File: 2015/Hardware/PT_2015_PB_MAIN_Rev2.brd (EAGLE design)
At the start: 137.2 x 166.4 mm, 135 parts, among them Q1 Q_ACS711LC, Q11 Q_IRFS7437PbF, Q12 2N7002, Q14 Q_IRFS7437PbF, Q16 Q_IRFS7437PbF, Q18 Q_FDT86102LZ, Q20 Q_IRFS7437PbF, Q4 Q_ACS711LC, Q5 Q_ACS711LC, Q6 Q_IRFS7437PbF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

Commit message: can't remember
made some small changes
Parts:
- moved C3 37.5 mm to (61.6, 80.0)
- moved C2 19.7 mm to (61.6, 60.3)
- moved C1 17.8 mm to (61.6, 42.5)
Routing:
- net PRIMARY-VMEAS: track 7.16 -> 8.20 mm
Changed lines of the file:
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@@
 <element name="VADER-5V-EXT" library="MRDT-2015-PowerBoard" package="R_PDSS-T7" value="Q_PTN78020WAH" x="103.505" y="88.9"/>
 <element name="DOOKU-12V-CRIT" library="MRDT-2015-PowerBoard" package="R_PDSS-T7" value="Q_PTN78020WAH" x="103.505" y="63.5"/>
-<element name="C1" library="MRDT-2014-All" package="C_12.5MM" value="1mF" x="61.595" y="60.325"/>
-<element name="C2" library="MRDT-2014-All" package="C_12.5MM" value="1mF" x="61.595" y="80.01"/>
-<element name="C3" library="MRDT-2014-All" package="C_12.5MM" value="1mF" x="61.595" y="42.545"/>
+<element name="C2" library="MRDT-2014-All" package="C_12.5MM" value="1mF" x="61.595" y="60.325"/>
+<element name="C3" library="MRDT-2014-All" package="C_12.5MM" value="1mF" x="61.595" y="80.01"/>
+<element name="C1" library="MRDT-2014-All" package="C_12.5MM" value="1mF" x="61.595" y="42.545"/>
 <element name="C4" library="MRDT-2014-All" package="C_12.5MM" value="1mF" x="60.96" y="103.505"/>
 <element name="C5" library="resistor" package="C1206" value=".1µF" x="45.72" y="1.778" rot="R180"/>
@@
 <contactref element="C15" pad="1"/>
 <contactref element="C4" pad="-"/>
+<contactref element="C1" pad="-"/>
 <contactref element="C3" pad="-"/>
 <contactref element="C2" pad="-"/>
-<contactref element="C1" pad="-"/>
 <contactref element="U$2" pad="2"/>
 <contactref element="C11" pad="2"/>
@@
 <contactref element="L5" pad="3"/>
 <contactref element="C10" pad="2"/>
-<contactref element="C1" pad="+"/>
 <contactref element="C2" pad="+"/>
 <contactref element="C3" pad="+"/>
+<contactref element="C1" pad="+"/>
 <contactref element="C4" pad="+"/>
 <contactref element="U$14" pad="1"/>
@@
 <wire x1="128.905" y1="11.43" x2="128.905" y2="27.94" width="1.016" layer="16"/>
 <via x="121.793" y="31.623" extent="1-16" drill="0.3302"/>
-<wire x1="121.793" y1="31.623" x2="105.41" y2="31.496" width="0.8128" layer="1"/>
-<wire x1="105.41" y1="31.496" x2="103.759" y2="33.147" width="0.8128" layer="1"/>
-<wire x1="103.759" y1="33.147" x2="103.759" y2="37.846" width="0.8128" layer="1"/>
+<wire x1="121.793" y1="31.623" x2="105.41" y2="31.623" width="0.8128" layer="1"/>
+<wire x1="105.41" y1="31.623" x2="103.759" y2="33.274" width="0.8128" layer="1"/>
+<wire x1="103.759" y1="33.274" x2="103.759" y2="37.846" width="0.8128" layer="1"/>
 <wire x1="103.759" y1="37.846" x2="102.362" y2="39.243" width="0.8128" layer="16"/>
 <wire x1="102.362" y1="39.243" x2="88.265" y2="39.243" width="0.8128" layer="16"/>
@@
 <contactref element="U$1" pad="19"/>
 <wire x1="82.067" y1="32.258" x2="84.938" y2="32.258" width="0.4064" layer="1"/>
-<wire x1="87.63" y1="29.083" x2="85.09" y2="31.623" width="0.4064" layer="1"/>
-<wire x1="85.09" y1="31.623" x2="85.09" y2="32.106" width="0.4064" layer="1"/>
 <wire x1="85.09" y1="32.106" x2="84.938" y2="32.258" width="0.4064" layer="1"/>
+<wire x1="85.09" y1="32.106" x2="85.09" y2="30.861" width="0.4064" layer="1"/>
+<wire x1="85.09" y1="30.861" x2="85.471" y2="30.48" width="0.4064" layer="1"/>
+<wire x1="85.471" y1="30.48" x2="87.249" y2="30.48" width="0.4064" layer="1"/>
+<wire x1="87.249" y1="30.48" x2="87.63" y2="30.099" width="0.4064" layer="1"/>
+<wire x1="87.63" y1="30.099" x2="87.63" y2="29.083" width="0.4064" layer="1"/>
 </signal>
 <signal name="M2-IMEAS">
@@
 <contactref element="Q5" pad="7"/>
 <contactref element="U$1" pad="1"/>
-<wire x1="120.65" y1="46.863" x2="123.825" y2="48.26" width="0.4064" layer="1"/>
-<wire x1="123.825" y1="48.26" x2="128.778" y2="48.26" width="0.4064" layer="1"/>
+<wire x1="120.65" y1="46.863" x2="122.047" y2="48.26" width="0.4064" layer="1"/>
+<wire x1="122.047" y1="48.26" x2="128.778" y2="48.26" width="0.4064" layer="1"/>
 <wire x1="128.778" y1="48.26" x2="130.175" y2="49.657" width="0.4064" layer="1"/>
 <wire x1="130.175" y1="49.657" x2="130.175" y2="53.915" width="0.4064" layer="1"/>

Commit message: Oh yeah BTW this is basically done
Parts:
- moved BATT-POS 0.25 mm to (62.4, 13.5)
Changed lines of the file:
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@@
 <element name="C10" library="resistor" package="C1206" value="" x="81.153" y="52.197" rot="R180"/>
 <element name="C14" library="resistor" package="C1206" value="2.2µF" x="81.28" y="68.58" rot="R270"/>
-<element name="BATT-POS" library="MRDT-2015-PowerBoard" package="LARGE_TERMINAL_HOLE" value="TERMINAL_HOLE" x="62.103" y="13.462"/>
+<element name="BATT-POS" library="MRDT-2015-PowerBoard" package="LARGE_TERMINAL_HOLE" value="TERMINAL_HOLE" x="62.357" y="13.462"/>
 <element name="BATT-NEG" library="MRDT-2015-PowerBoard" package="LARGE_TERMINAL_HOLE" value="TERMINAL_HOLE" x="93.98" y="13.462"/>
 <element name="Q6" library="MRDT-2015-PowerBoard" package="D2PACK" value="Q_IRFS7437PbF" x="29.21" y="7.62" rot="R270"/>

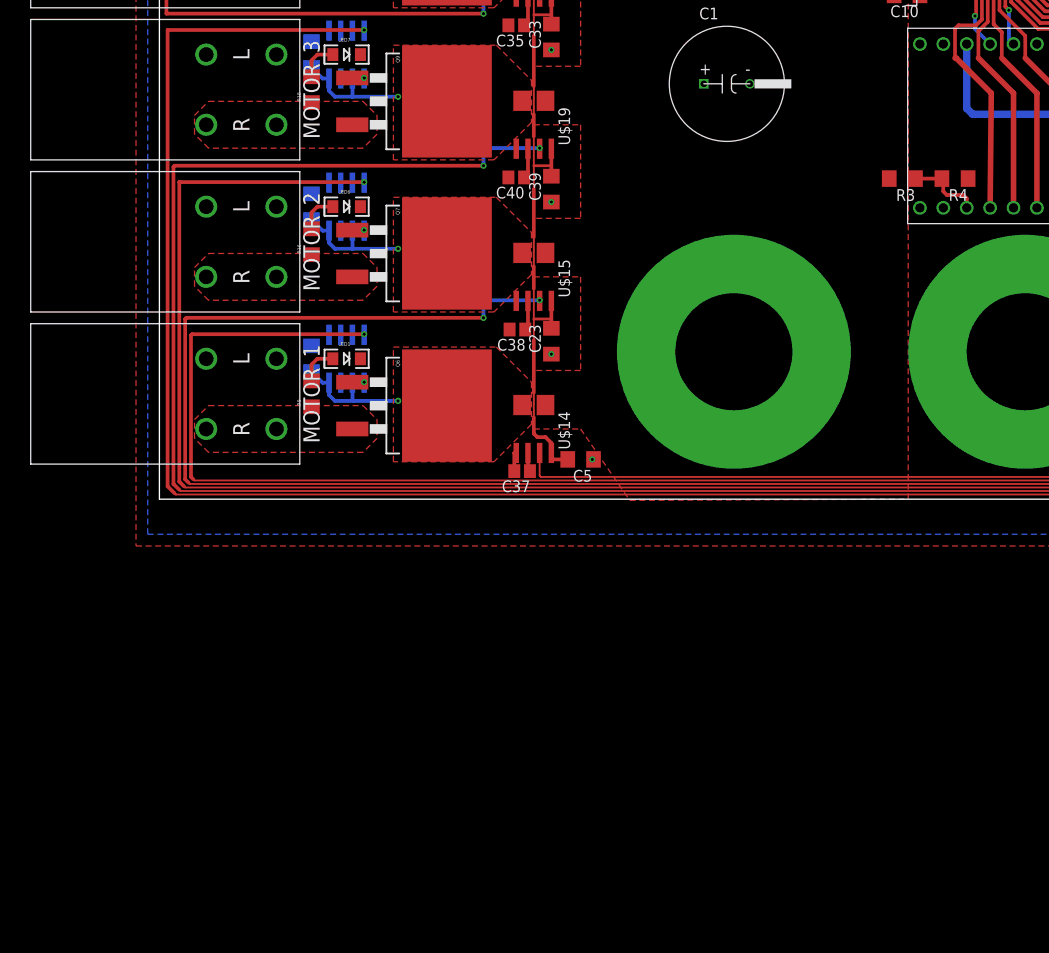
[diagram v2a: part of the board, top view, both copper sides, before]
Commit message: Added a buzzer and LEDs to schematic
Parts are not placed yet.
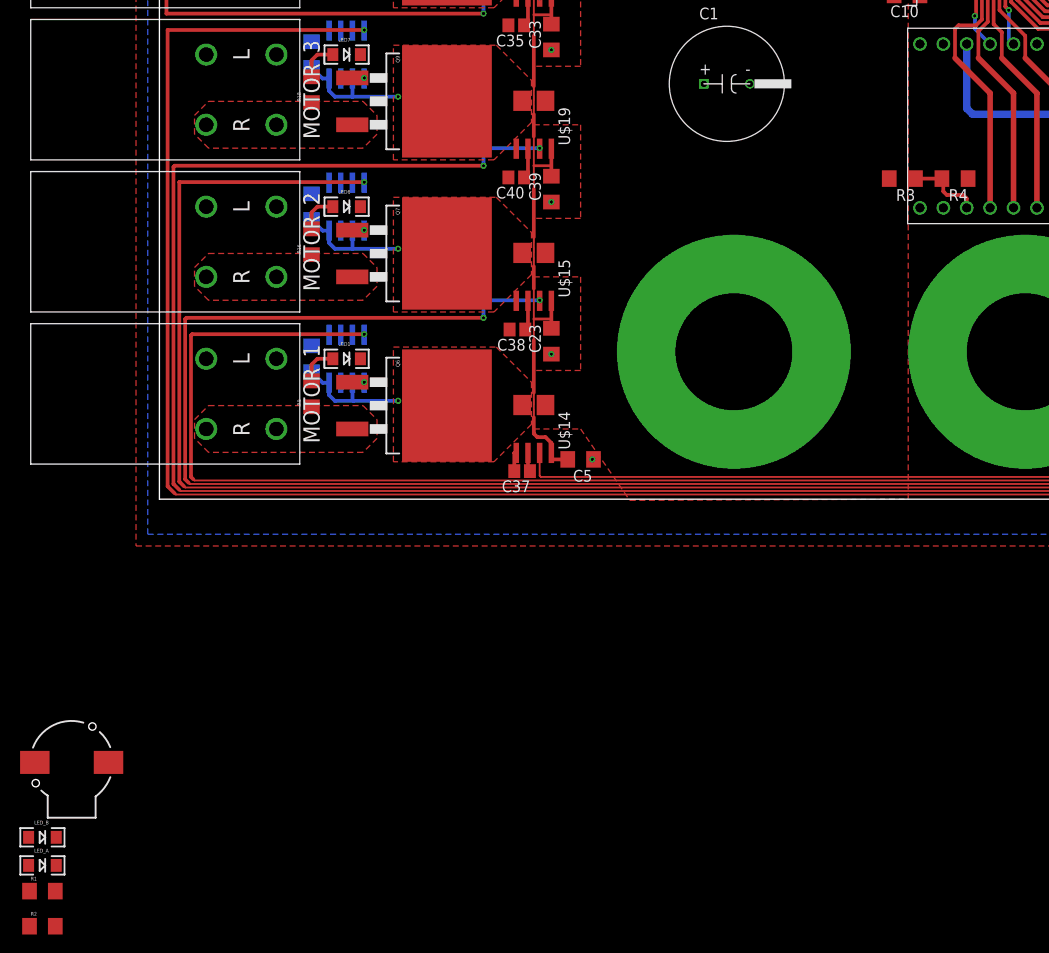
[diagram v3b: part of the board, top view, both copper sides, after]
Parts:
- added LED_A, LED_B: (no value), SparkFun-LED:LED-1206
- added R1, R2: 1kΩ, SparkFun-Passives:1206
- added SG1: BUZZERSMD2, SparkFun-Electromechanical:BUZZER-CCV
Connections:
- new net BUZZER: SG1.+, U$1.11
- new net LED_A: R1.1, U$1.9
- new net LED_B: R2.1, U$1.10
- new net N$32: LED_A.A, R1.2
- new net N$33: LED_B.A, R2.2
- net GND: now also LED_A.C, LED_B.C, SG1.-
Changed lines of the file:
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@@
 <attribute name="DIGIKEY_PN" value="732-2769-ND" x="-128.143" y="-38.735" size="1.778" layer="27" rot="R270" display="off"/>
 </element>
+<element name="SG1" library="SparkFun-Electromechanical" package="BUZZER-CCV" value="BUZZERSMD2" x="-9.525" y="-31.115"/>
+<element name="LED_B" library="SparkFun-LED" package="LED-1206" value="" x="-12.7" y="-39.243"/>
+<element name="LED_A" library="SparkFun-LED" package="LED-1206" value="" x="-12.7" y="-42.291"/>
+<element name="R1" library="SparkFun-Passives" package="1206" value="1kΩ" x="-12.7" y="-45.085"/>
+<element name="R2" library="SparkFun-Passives" package="1206" value="1kΩ" x="-12.7" y="-48.895"/>
 </elements>
 <signals>
@@
 <wire x1="38.735" y1="2.48" x2="38.52" y2="2.48" width="0.4064" layer="1"/>
 <wire x1="38.52" y1="2.48" x2="38.52" y2="0.508" width="0.4064" layer="1"/>
+<contactref element="SG1" pad="-"/>
+<contactref element="LED_A" pad="C"/>
+<contactref element="LED_B" pad="C"/>
+<wire x1="-11.2" y1="-39.243" x2="-11.2" y2="-42.291" width="0" layer="19" extent="1-1"/>
+<wire x1="-13.525" y1="-31.115" x2="-11.2" y2="-39.243" width="0" layer="19" extent="1-1"/>
+<wire x1="5.08" y1="12.7" x2="-13.525" y2="-31.115" width="0" layer="19" extent="1-1"/>
 </signal>
 <signal name="V_BATT">
@@
 <wire x1="86.741" y1="48.895" x2="86.36" y2="48.514" width="0.4064" layer="1"/>
 <wire x1="86.36" y1="48.514" x2="86.36" y2="45.339" width="0.4064" layer="1"/>
-<wire x1="90.17" y1="29.083" x2="90.297" y2="41.529" width="0.6096" layer="1"/>
-<wire x1="90.297" y1="41.529" x2="86.487" y2="45.339" width="0.6096" layer="1"/>
-<wire x1="86.487" y1="45.339" x2="86.36" y2="45.339" width="0.6096" layer="1"/>
+<wire x1="90.17" y1="29.083" x2="90.17" y2="41.529" width="0.6096" layer="1"/>
+<wire x1="90.17" y1="41.529" x2="86.36" y2="45.339" width="0.6096" layer="1"/>
 <wire x1="103.378" y1="100.33" x2="102.616" y2="99.568" width="0.4064" layer="1"/>
 <wire x1="67.945" y1="141.351" x2="67.183" y2="140.589" width="0.4064" layer="1"/>
@@
 <signal name="N$13">
 </signal>
+<signal name="BUZZER">
+<contactref element="SG1" pad="+"/>
+<contactref element="U$1" pad="11"/>
+<wire x1="-5.525" y1="-31.115" x2="95.25" y2="46.863" width="0" layer="19" extent="1-1"/>
+</signal>
+<signal name="N$32">
+<contactref element="LED_A" pad="A"/>
+<contactref element="R1" pad="2"/>
+<wire x1="-11.3" y1="-45.085" x2="-14.2" y2="-42.291" width="0" layer="19" extent="1-1"/>
+</signal>
+<signal name="N$33">
+<contactref element="LED_B" pad="A"/>
+<contactref element="R2" pad="2"/>
+<wire x1="-14.2" y1="-39.243" x2="-11.3" y2="-48.895" width="0" layer="19" extent="1-1"/>
+</signal>
+<signal name="LED_B">
+<contactref element="U$1" pad="10"/>
+<contactref element="R2" pad="1"/>
+<wire x1="-14.1" y1="-48.895" x2="97.79" y2="46.863" width="0" layer="19" extent="1-1"/>
+</signal>
+<signal name="LED_A">
+<contactref element="U$1" pad="9"/>
+<contactref element="R1" pad="1"/>
+<wire x1="-14.1" y1="-45.085" x2="100.33" y2="46.863" width="0" layer="19" extent="1-1"/>
+</signal>
 </signals>

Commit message: Fixed the triangle thing
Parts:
- removed LED_A, LED_B: (no value), SparkFun-LED:LED-1206
- removed R1, R2: 1kΩ, SparkFun-Passives:1206
- removed SG1: BUZZERSMD2, SparkFun-Electromechanical:BUZZER-CCV
- moved C3 37.5 mm to (61.6, 42.5)
- moved C2 19.7 mm to (61.6, 80.0)
- moved C1 17.8 mm to (61.6, 60.3)
- moved BATT-POS 0.25 mm to (62.1, 13.5)
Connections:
- removed net BUZZER: SG1.+, U$1.11
- removed net LED_A: R1.1, U$1.9
- removed net LED_B: R2.1, U$1.10
- removed net N$32: LED_A.A, R1.2
- removed net N$33: LED_B.A, R2.2
- net GND: no longer LED_A.C, LED_B.C, SG1.-
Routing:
- net ARM_P-SIG: track 220.4 -> 211.9 mm
- net ARM_P-IMEAS: track 292.3 -> 285.0 mm
- net AUX_P-IMEAS: track 316.7 -> 310.2 mm
- net M6-IMEAS: track 335.3 -> 329.7 mm
- net M5-IMEAS: track 354.7 -> 350.1 mm
- net M4-IMEAS: track 386.4 -> 382.7 mm
- net AUX_P-SIG: track 282.8 -> 280.2 mm
- net GND: track 2.32 -> 0.13 mm
- net M6-SIG: track 306.1 -> 304.5 mm
- net PRIMARY-VMEAS: track 8.20 -> 7.16 mm
- net M5-SIG: track 326.8 -> 326.3 mm

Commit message: init commit
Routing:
- net ARM_P-SIG: track 211.9 -> 185.9 mm
- net ARM_P-IMEAS: track 285.0 -> 259.2 mm
- net AUX_P-IMEAS: track 310.2 -> 284.6 mm
- net M6-IMEAS: track 329.7 -> 304.4 mm
- net M5-IMEAS: track 350.1 -> 325.0 mm
- net M4-IMEAS: track 382.7 -> 357.8 mm
- net AUX_P-SIG: track 280.2 -> 255.4 mm
- net M6-SIG: track 304.5 -> 280.3 mm
- net M5-SIG: track 326.3 -> 302.5 mm
- net +5V: track 629.7 -> 606.3 mm
- net 12V-IMEAS: track 289.1 -> 284.3 mm
- net M4-SIG: track 352.8 -> 350.4 mm
- net GND: vias 26 -> 16
- removed copper zone on layer 1, net N$7

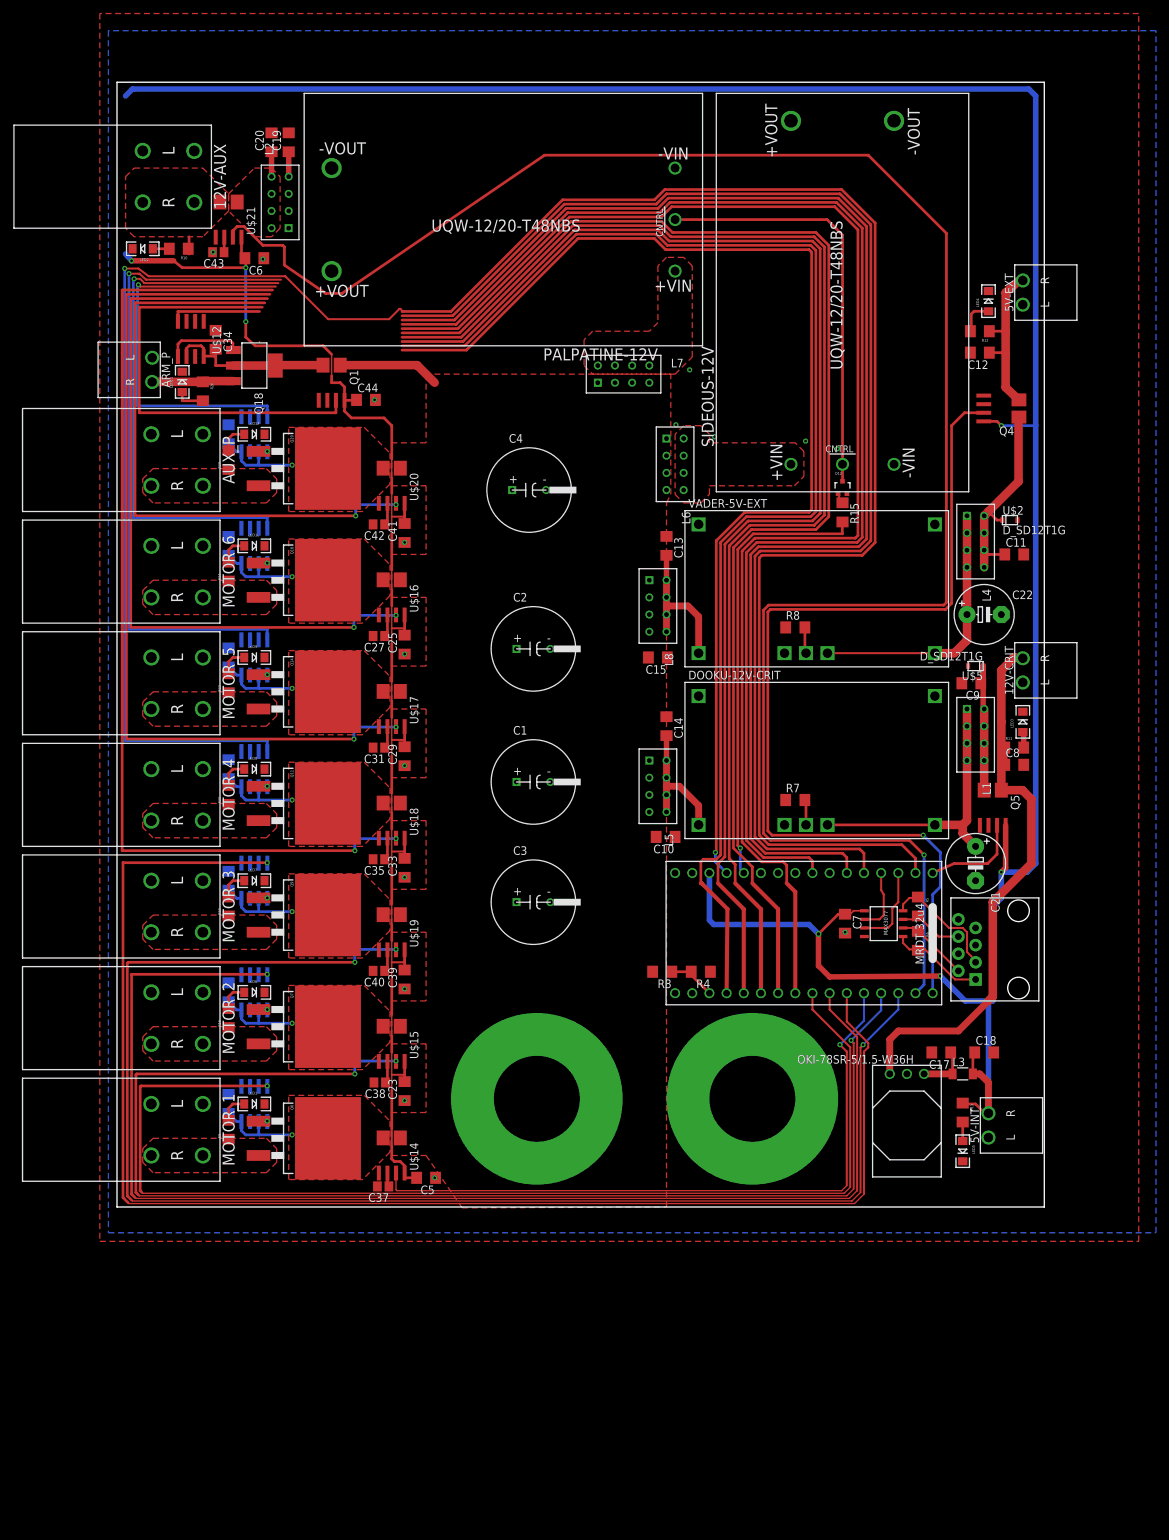
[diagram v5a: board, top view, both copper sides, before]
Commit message: rou
is my eagle command for route because fuck buttons.
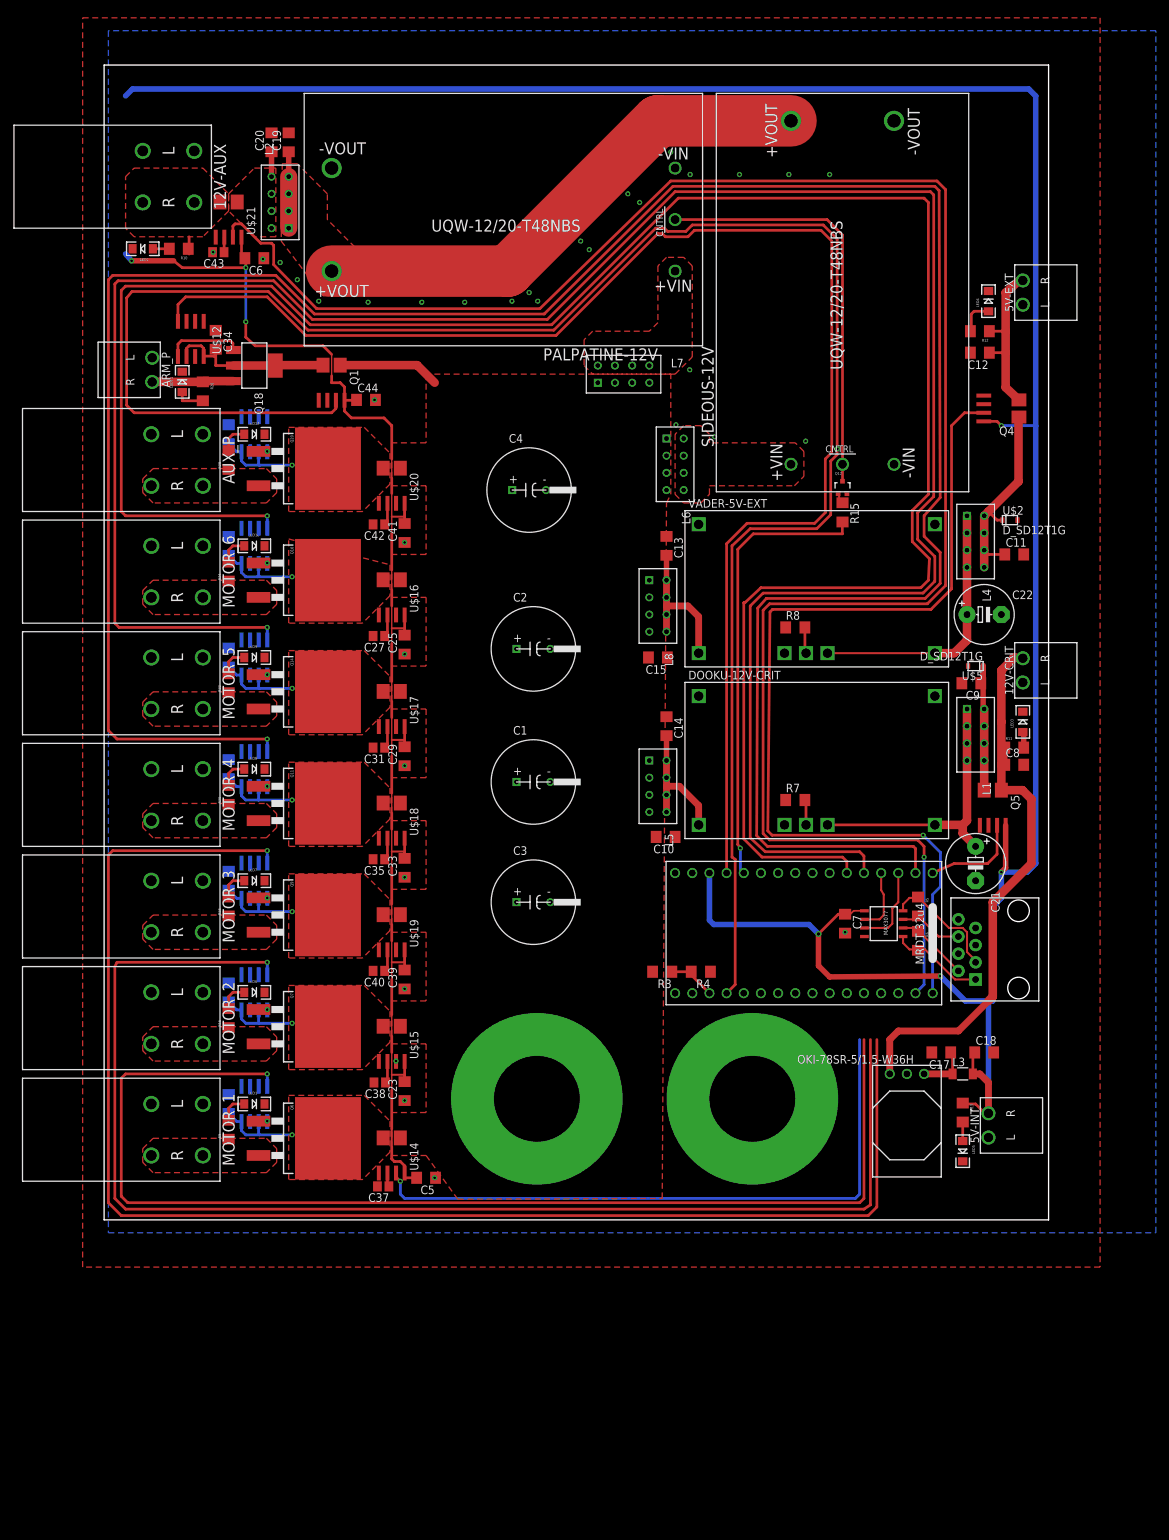
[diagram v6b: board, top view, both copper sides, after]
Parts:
- R7: value 585Ω -> 590Ω
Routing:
- net M4-IMEAS: track 357.8 -> 0.00 mm, vias 2 -> 0
- net M5-IMEAS: track 325.0 -> 0.00 mm, vias 2 -> 0
- net M6-IMEAS: track 304.4 -> 0.00 mm, vias 2 -> 0
- net AUX_P-IMEAS: track 284.6 -> 0.00 mm, vias 2 -> 0
- net AUX_P-SIG: track 255.4 -> 0.00 mm, vias 1 -> 0
- net M3-IMEAS: track 217.3 -> 0.00 mm, vias 3 -> 0
- net M2-IMEAS: track 195.7 -> 0.00 mm, vias 3 -> 0
- net N$7: track 3.68 -> 88.5 mm
- net M5-SIG: track 302.5 -> 349.2 mm
- net M6-SIG: track 280.3 -> 326.3 mm
- net ARM_P-IMEAS: track 259.2 -> 288.9 mm
- net ARM_P-SIG: track 185.9 -> 215.3 mm, vias 1 -> 0
- net M4-SIG: track 350.4 -> 376.2 mm
- net M1-IMEAS: track 99.9 -> 94.7 mm
- net 12V-IMEAS: track 284.3 -> 289.3 mm
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- added copper zone on layer 1, net N$7
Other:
- board size 137.2 x 166.4 mm -> 139.7 x 170.8 mm
